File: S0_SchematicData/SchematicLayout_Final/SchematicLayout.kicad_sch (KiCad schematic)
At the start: 9 parts, among them P1 Conn_Plug_2P, Q1 Q_NMOS, Q2 Q_NMOS, Q3 Q_NMOS, Q4 Q_NMOS, U1 LMZM23600V5, U2 ESP32-S2-WROVER

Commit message: Sync and commit of current C code
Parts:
- removed Q1, Q2, Q3: Q_NMOS, symbol Device:Q_NMOS
- removed U2: ESP32-S2-WROVER, RF_Module:ESP32-S2-WROVER, symbol RF_Module:ESP32-S2-WROVER
- added U2: ESP32-WROOM-32D, RF_Module:ESP32-WROOM-32D, symbol RF_Module:ESP32-WROOM-32D
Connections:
- net at U1.1 (GND), U1.11 (GND): now also U2.1 (GND), U2.15 (GND), U2.38 (GND), U2.39 (GND); no longer Q4.D
- net at U1.6 (VOUT): now also U2.2 (VDD)
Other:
- note added: "LINK: Pinout for this devboard"
- note removed: "Aeurbach"
- note removed: "Dundee"
- note removed: "Salina"
- note removed: "Vancouver"
- moved on the sheet: BT1, Button_PatternLED, P1, Q4, U1

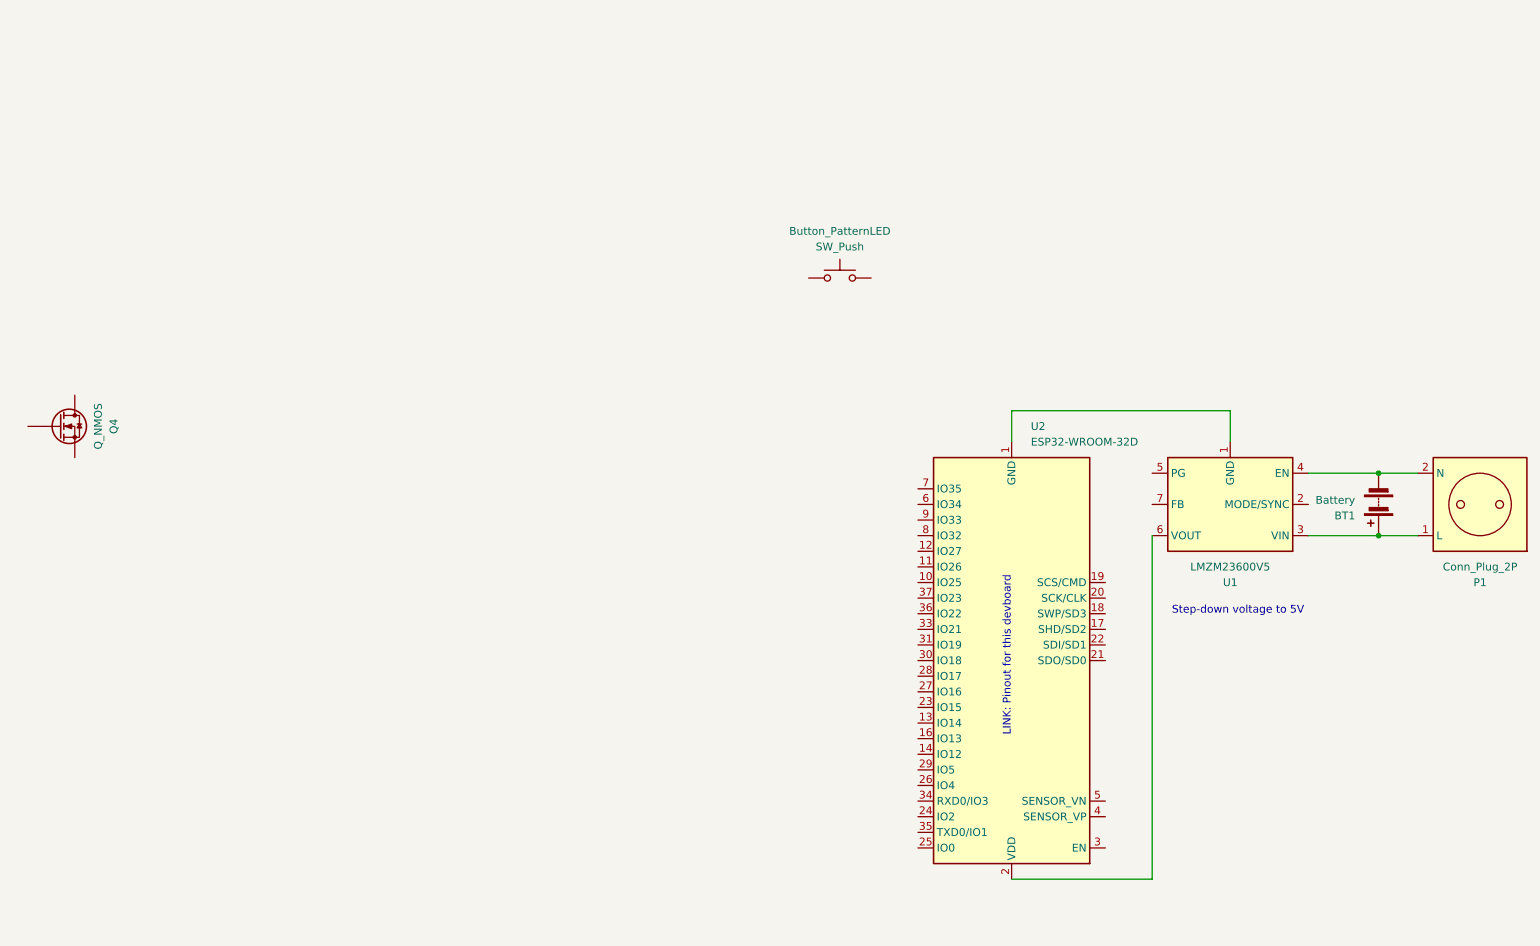
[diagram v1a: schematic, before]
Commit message: Schematic with correct N-Mosfet wiring created
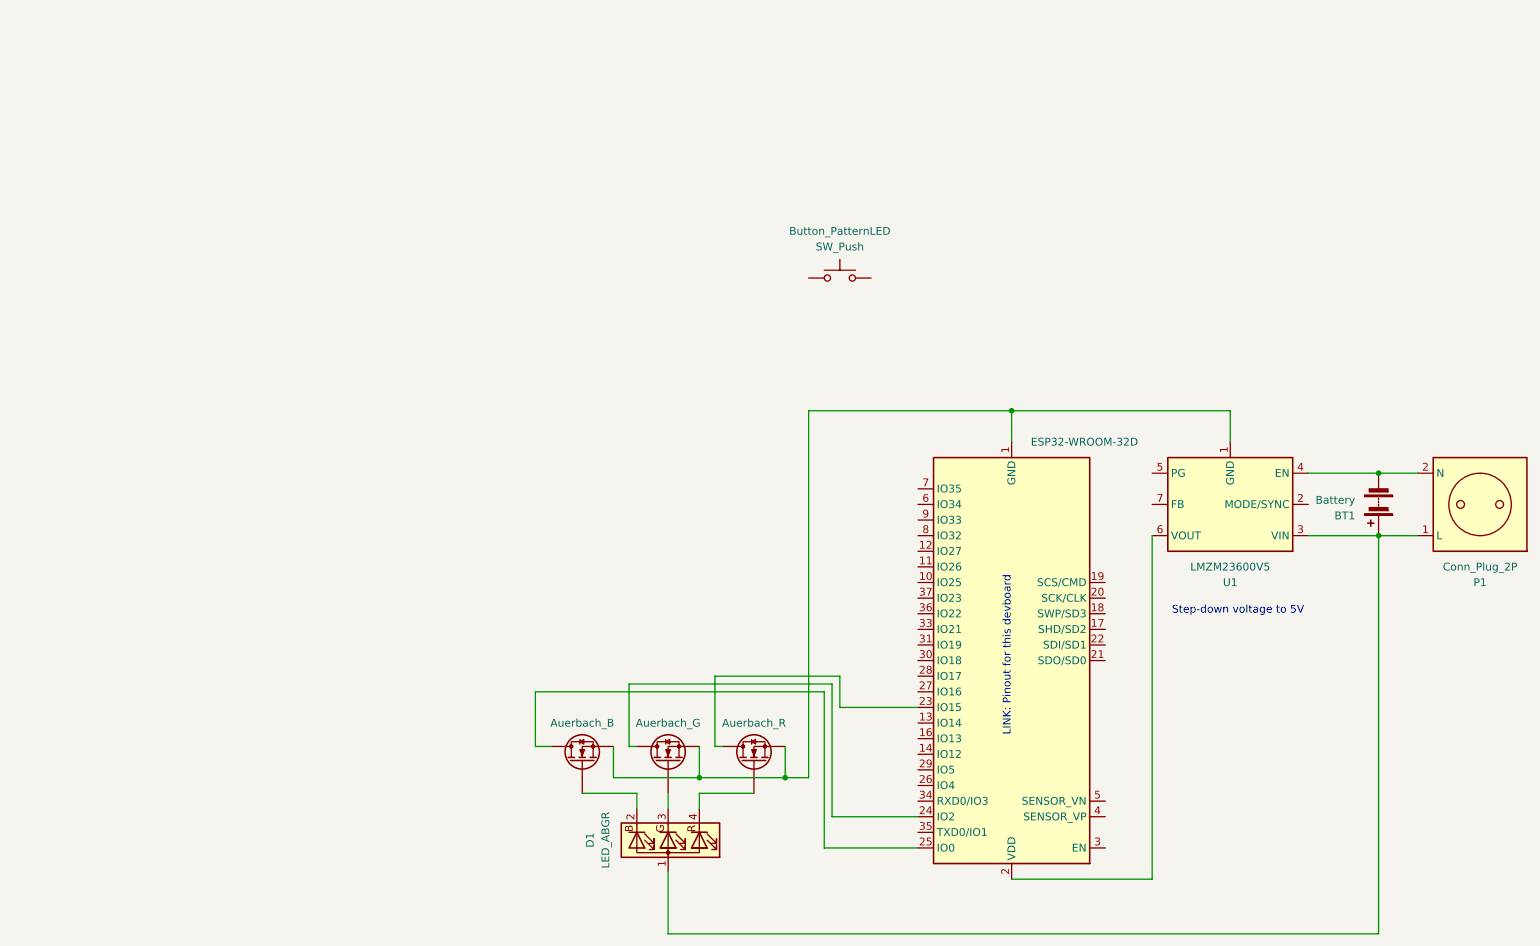
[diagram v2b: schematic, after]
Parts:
- added D1: LED_ABGR, symbol Device:LED_ABGR
- added Q5: Auerbach_G, symbol Device:Q_NMOS
- added Q6: Auerbach_B, symbol Device:Q_NMOS
- Q4: value Q_NMOS -> Auerbach_R
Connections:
- net at U1.1 (GND), U1.11 (GND), U2.1 (GND)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: now also Q4.S, Q5.S, Q6.S
- net at BT1.1 (+), P1.1 (L), U1.3 (VIN): now also D1.1 (A)
- net at U2.23 (IO15): now also Q4.D
- net at U2.24 (IO2): now also Q5.D
- net at U2.25 (IO0): now also Q6.D
- net at Q4.G: now also D1.4 (RK)
- new net: D1.2 (BK), Q6.G
- new net: D1.3 (GK), Q5.G

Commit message: Completion of schematic
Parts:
- added D2, D3, D4: LED_ABGR, symbol Device:LED_ABGR
- added Q10: Dundee_B, symbol Device:Q_NMOS
- added Q11: Dundee_G, symbol Device:Q_NMOS
- added Q12: Dundee_R, symbol Device:Q_NMOS
- added Q13: Vancouver_R, symbol Device:Q_NMOS
- added Q14: Vancouver_G, symbol Device:Q_NMOS
- added Q15: Vancouver_B, symbol Device:Q_NMOS
- added Q7: Salina_B, symbol Device:Q_NMOS
- added Q8: Salina_G, symbol Device:Q_NMOS
- added Q9: Salina_R, symbol Device:Q_NMOS
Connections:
- net at Q4.S, Q5.S, Q6.S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: now also Q10.S, Q11.S, Q12.S, Q13.S, Q14.S, Q15.S, Q7.S, Q8.S, Q9.S
- net at BT1.1 (+), D1.1 (A), P1.1 (L)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: now also D2.1 (A), D3.1 (A), D4.1 (A)
- net at U2.26 (IO4): now also Q9.D
- net at U2.27 (IO16): now also Q8.D
- net at U2.28 (IO17): now also Q7.D
- net at U2.29 (IO5): now also Q12.D
- net at U2.30 (IO18): now also Q11.D
- net at U2.31 (IO19): now also Q10.D
- net at U2.33 (IO21): now also Q13.D
- net at U2.34 (RXD0/IO3): now also Q14.D
- net at U2.35 (TXD0/IO1): now also Q15.D
- new net: D2.4 (RK), Q9.G
- new net: D4.2 (BK), Q15.G
- new net: D4.3 (GK), Q14.G
- new net: D4.4 (RK), Q13.G
- new net: D3.3 (GK), Q11.G
- new net: D3.2 (BK), Q10.G
- new net: D2.2 (BK), Q7.G
- new net: D2.3 (GK), Q8.G
- new net: D3.4 (RK), Q12.G
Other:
- note added: "12v Main LED Power"
- note added: "Absolute rats nest, but this is needed to achieve the desired PWM control of LED strips"
- note added: "Grounding through the ESP32 is safe"
- moved on the sheet: BT1, Button_PatternLED, D1, P1, U1

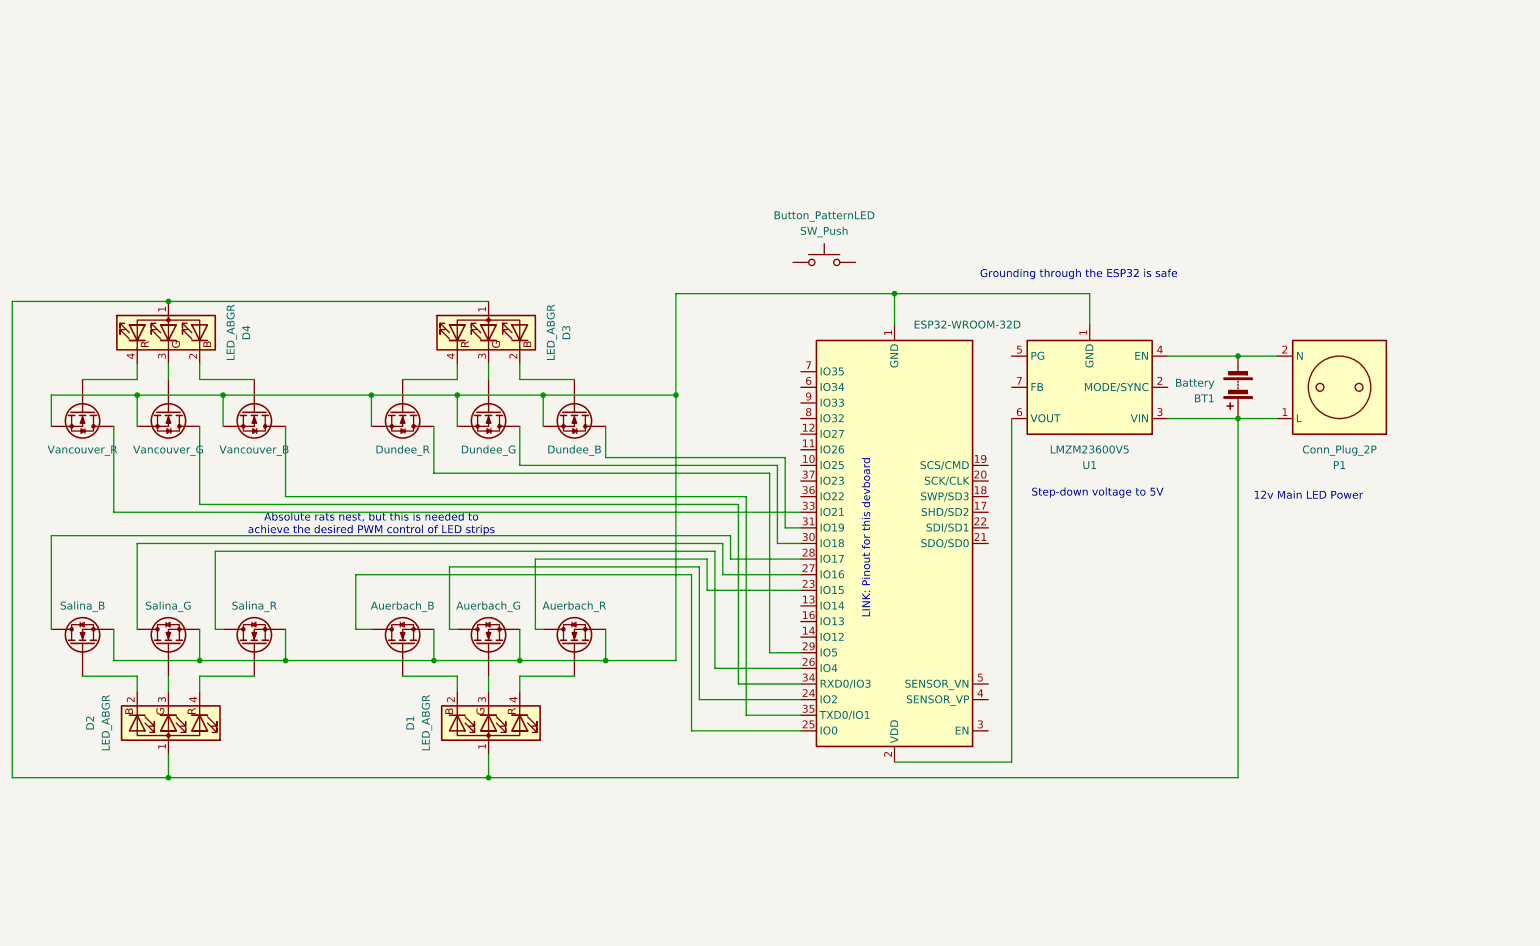
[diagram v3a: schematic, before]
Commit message: Alteration of schematic layout and LED power scaling introdution
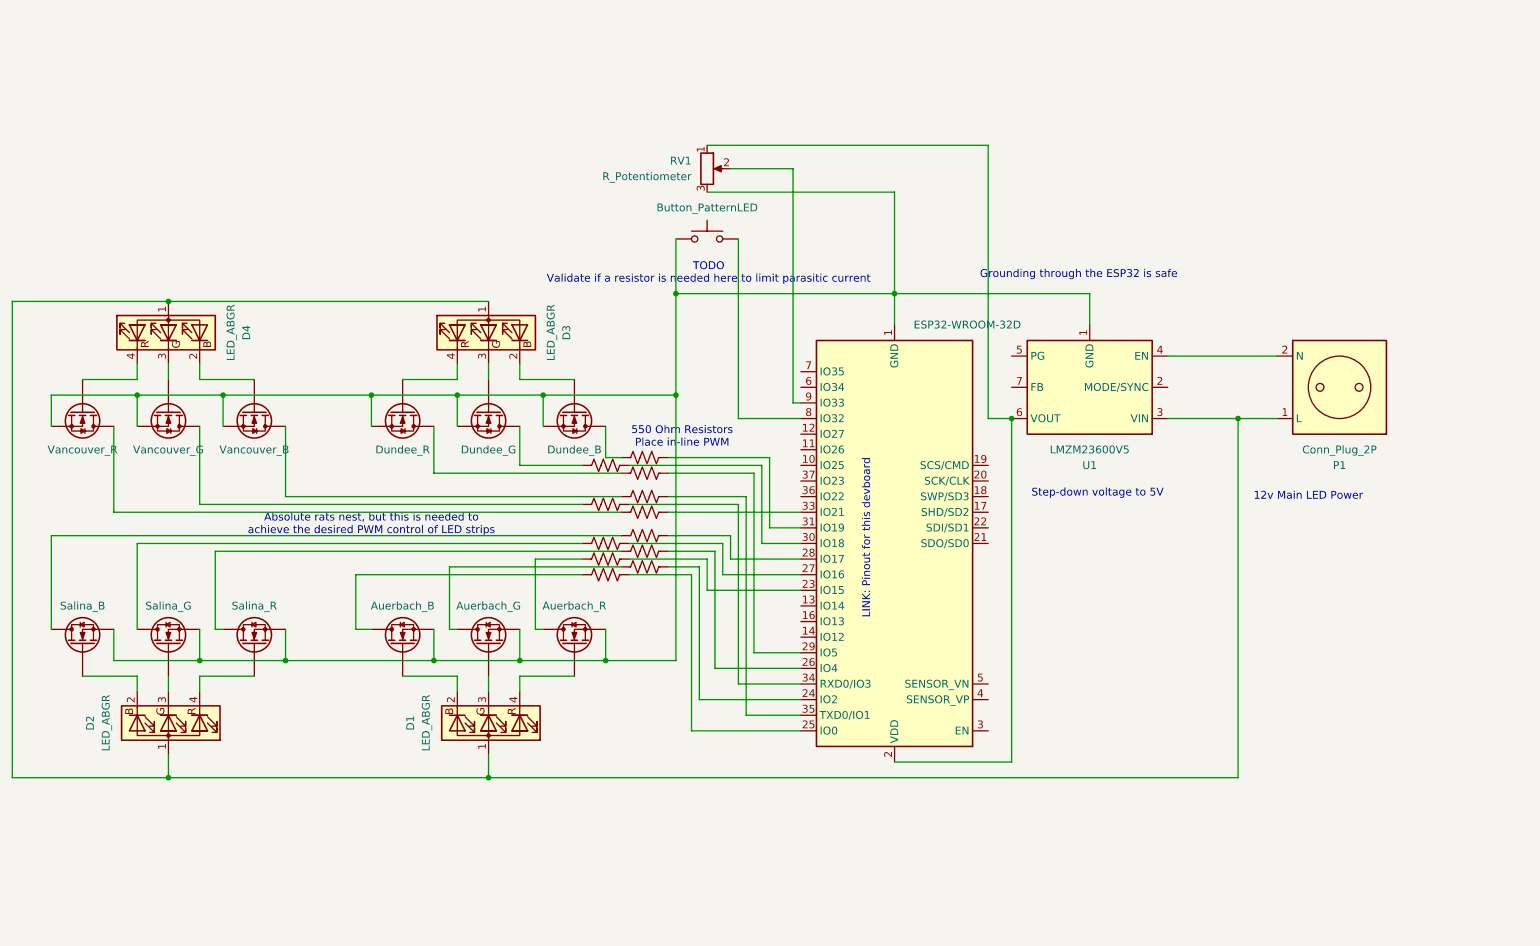
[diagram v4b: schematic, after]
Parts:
- removed BT1: Battery, symbol Device:Battery
- added R1, R10, R11, R12, R2, R3, R4, R5, R6, R7, R8, R9: R_US, symbol Device:R_US
- added RV1: R_Potentiometer, symbol Device:R_Potentiometer
- Button_PatternLED: value SW_Push -> Button_PatternLED
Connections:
- net at Q6.D: now also R6.1; no longer U2.25 (IO0)
- net at Q10.S, Q11.S, Q12.S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: now also Button_PatternLED.1, RV1.3
- net at Q9.D: now also R3.1; no longer U2.26 (IO4)
- net at Q5.D: now also R5.1; no longer U2.24 (IO2)
- net at Button_PatternLED.2: now also U2.8 (IO32)
- net at U1.6 (VOUT), U2.2 (VDD): now also RV1.1
- net at Q4.D: now also R4.1; no longer U2.23 (IO15)
- net at Q8.D: now also R2.1; no longer U2.27 (IO16)
- net at U2.28 (IO17): now also R1.2; no longer Q7.D
- net at Q12.D: now also R10.1; no longer U2.29 (IO5)
- net at U2.30 (IO18): now also R11.2; no longer Q11.D
- net at U2.31 (IO19): now also R12.2; no longer Q10.D
- net at Q13.D: now also R7.1; no longer U2.33 (IO21)
- net at U2.34 (RXD0/IO3): now also R8.2; no longer Q14.D
- net at U2.35 (TXD0/IO1): now also R9.2; no longer Q15.D
- net at U2.9 (IO33): now also RV1.2
- new net: R10.2, U2.29 (IO5)
- new net: R2.2, U2.27 (IO16)
- new net: R3.2, U2.26 (IO4)
- new net: R7.2, U2.33 (IO21)
- new net: R4.2, U2.23 (IO15)
- new net: R5.2, U2.24 (IO2)
- new net: R6.2, U2.25 (IO0)
- new net: Q15.D, R9.1
- new net: Q11.D, R11.1
- new net: Q10.D, R12.1
- new net: Q14.D, R8.1
- new net: Q7.D, R1.1
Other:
- note added: "550 Ohm Resistors Place in-line PWM"
- note added: "TODO Validate if a resistor is needed here to limit parasitic current"
